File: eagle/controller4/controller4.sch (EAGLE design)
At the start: 70 parts, among them Q1 check_pins, Q2 FDD4141TO252, X1 1501_04, X2 ZX62D-B-5PA8

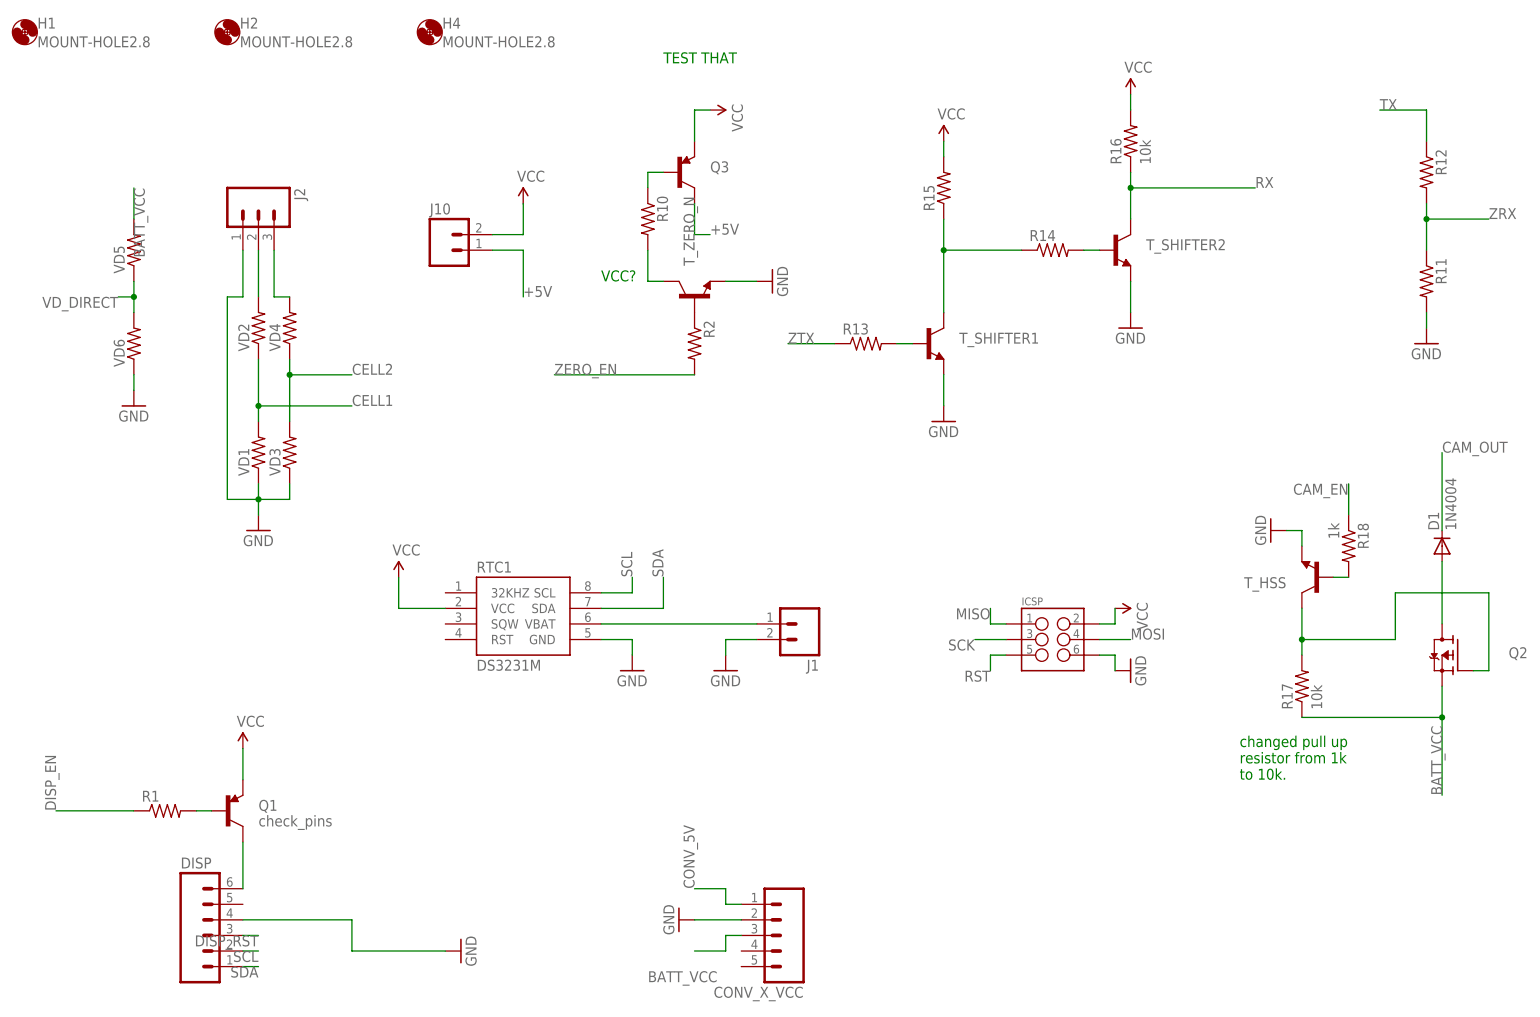
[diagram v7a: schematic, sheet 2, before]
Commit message: controller4: temp sensor and silkscreen
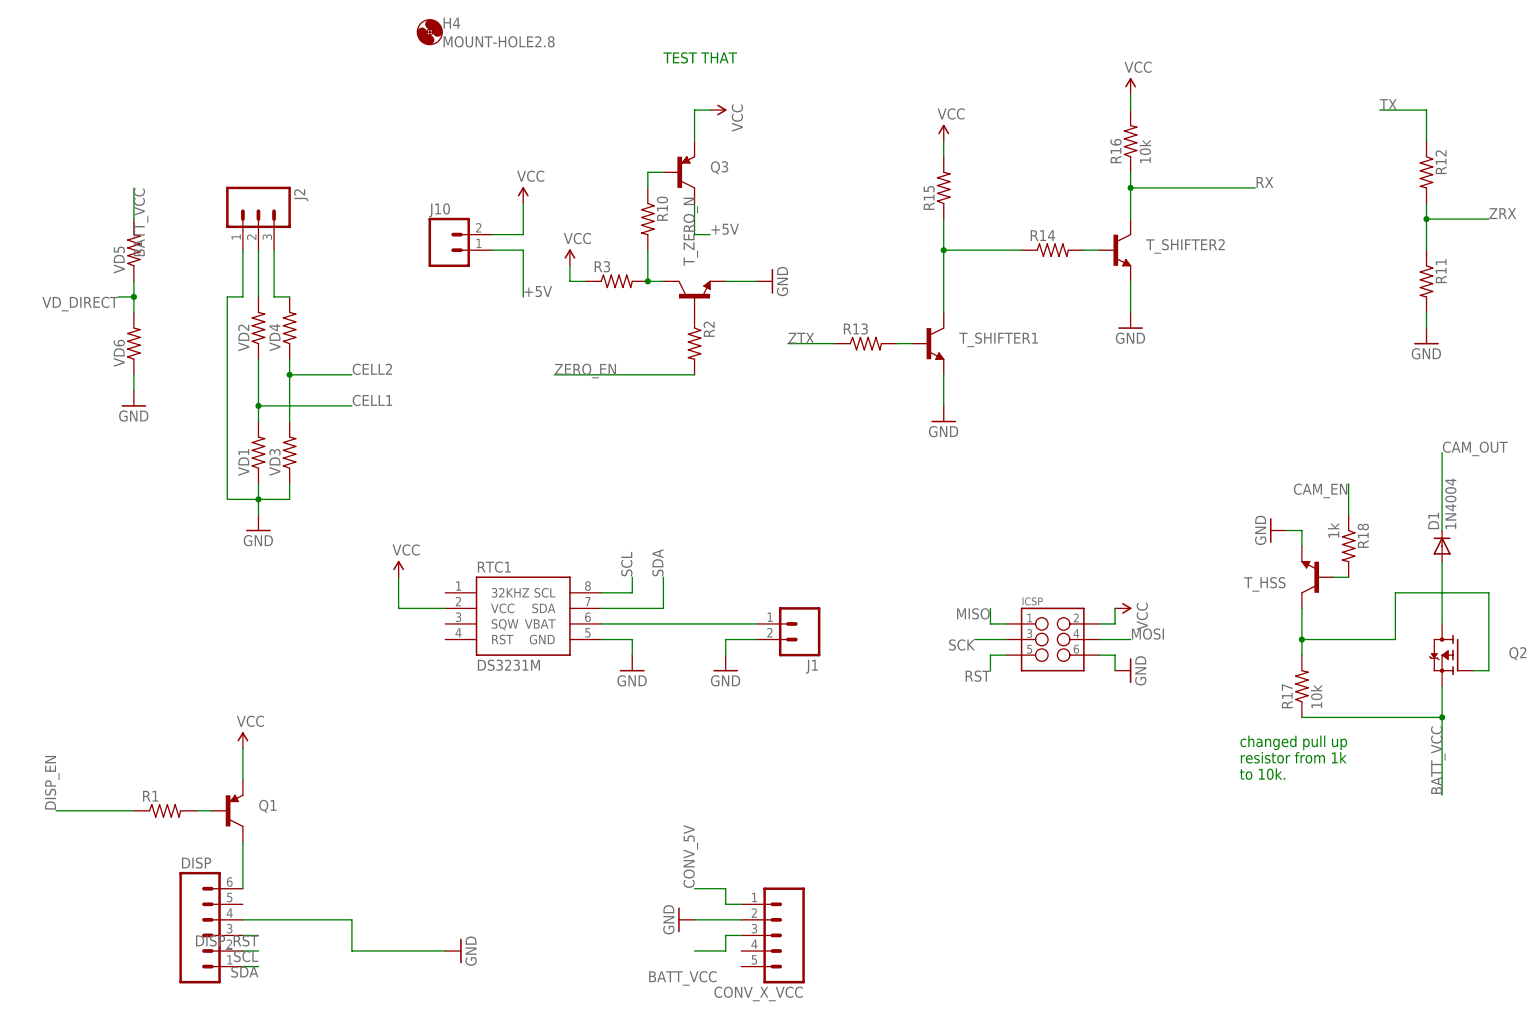
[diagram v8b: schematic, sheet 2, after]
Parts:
- removed H1, H2: MOUNT-HOLE2.8, holes:MOUNT-HOLE2.8
- added R3: (no value), SparkFun-Resistors:RESISTOR1206
- Q1: value check_pins -> (none)
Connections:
- net N$18: now also R3.2
- net VCC: now also R3.1
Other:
- note removed: "VCC?"
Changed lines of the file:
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@@
 <part name="SUPPLY3" library="SparkFun-Aesthetics" deviceset="VCC" device=""/>
 <part name="GND6" library="SparkFun-Aesthetics" deviceset="GND" device=""/>
-<part name="H2" library="holes" deviceset="MOUNT-HOLE" device="2.8" value="MOUNT-HOLE2.8"/>
 <part name="SUPPLY7" library="SparkFun-Aesthetics" deviceset="VCC" device=""/>
 <part name="SUPPLY8" library="SparkFun-Aesthetics" deviceset="VCC" device=""/>
@@
 <part name="Y1" library="SparkFun-FreqCtrl" deviceset="CRYSTAL" device="HC49US"/>
 <part name="S2" library="SparkFun-Electromechanical" deviceset="SWITCH-SPDT" device="PTH_LOCK"/>
-<part name="Q1" library="SparkFun-DiscreteSemi" deviceset="TRANSISTOR_PNP" device="TO92" value="check_pins"/>
+<part name="Q1" library="SparkFun-DiscreteSemi" deviceset="TRANSISTOR_PNP" device="TO92"/>
 <part name="R1" library="SparkFun-Resistors" deviceset="RESISTOR" device="1206"/>
 <part name="SUPPLY9" library="SparkFun-Aesthetics" deviceset="VCC" device=""/>
@@
 <part name="R2" library="SparkFun-Resistors" deviceset="RESISTOR" device="1206"/>
 <part name="GND27" library="SparkFun-Aesthetics" deviceset="GND" device=""/>
-<part name="H1" library="holes" deviceset="MOUNT-HOLE" device="2.8" value="MOUNT-HOLE2.8"/>
 <part name="FRAME2" library="frames" deviceset="DINA4_L" device=""/>
+<part name="R3" library="SparkFun-Resistors" deviceset="RESISTOR" device="1206"/>
+<part name="SUPPLY15" library="SparkFun-Aesthetics" deviceset="VCC" device=""/>
 </parts>
 <sheets>
@@
 resistor from 1k
 to 10k. </text>
-<text x="104.14" y="129.54" size="1.778" layer="91">VCC?</text>
 </plain>
 <instances>
@@
 <instance part="FRAME2" gate="G$2" x="162.56" y="0"/>
 <instance part="GND6" gate="1" x="48.26" y="88.9"/>
-<instance part="H2" gate="G$1" x="43.18" y="170.18"/>
 <instance part="CONV_X_VCC" gate="G$1" x="134.62" y="22.86" rot="R180"/>
 <instance part="GND17" gate="1" x="116.84" y="25.4" rot="R270"/>
@@
 <instance part="GND7" gate="1" x="124.46" y="66.04"/>
 <instance part="D1" gate="1" x="241.3" y="86.36" rot="R90"/>
-<instance part="H1" gate="G$1" x="10.16" y="170.18"/>
+<instance part="R3" gate="G$1" x="106.68" y="129.54"/>
+<instance part="SUPPLY15" gate="G$1" x="99.06" y="132.08"/>
 </instances>
 <busses>
@@
 <wire x1="71.12" y1="76.2" x2="71.12" y2="81.28" width="0.1524" layer="91"/>
 <pinref part="SUPPLY6" gate="G$1" pin="VCC"/>
+</segment>
+<segment>
+<pinref part="R3" gate="G$1" pin="1"/>
+<wire x1="101.6" y1="129.54" x2="99.06" y2="129.54" width="0.1524" layer="91"/>
+<pinref part="SUPPLY15" gate="G$1" pin="VCC"/>
+<wire x1="99.06" y1="129.54" x2="99.06" y2="132.08" width="0.1524" layer="91"/>
 </segment>
 </net>
@@
 <wire x1="114.3" y1="129.54" x2="111.76" y2="129.54" width="0.1524" layer="91"/>
 <wire x1="111.76" y1="129.54" x2="111.76" y2="134.62" width="0.1524" layer="91"/>
-</segment>
-</net>
+<pinref part="R3" gate="G$1" pin="2"/>
+<junction x="111.76" y="129.54"/>
+</segment>
+</net>
